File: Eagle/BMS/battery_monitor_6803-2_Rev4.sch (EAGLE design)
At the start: 66 parts, among them Q1 MOSFET-PCHANNELIRLML2244, Q10 IRF9530, Q2 MOSFET-NCHANNELBSS138, Q3 MOSFET-PCHANNELIRLML2244, Q4 MOSFET-PCHANNELIRLML2244, Q5 MOSFET-PCHANNELIRLML2244, Q6 MOSFET-NCHANNELBSS138, Q7 MOSFET-NCHANNELBSS138, Q8 MOSFET-NCHANNELBSS138, Q9 PMOS_AO4435

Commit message: Finished new BMS boards in Eagle.
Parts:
- U$9: MPN (none) -> LTC6803IG-2#PBF; OC_NEWARK (none) -> 27T5837
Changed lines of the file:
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@@
 </part>
 <part name="SUPPLY19" library="supply2" deviceset="GND" device=""/>
-<part name="U$9" library="Clayton" deviceset="LTC6803_BREAKOUT" device="" value="LTC6803"/>
+<part name="U$9" library="Clayton" deviceset="LTC6803_BREAKOUT" device="" value="LTC6803">
+<attribute name="MF" value=""/>
+<attribute name="MPN" value="LTC6803IG-2#PBF"/>
+<attribute name="OC_NEWARK" value="27T5837"/>
+</part>
 </parts>
 <sheets>
@@
 </instance>
 <instance part="SUPPLY19" gate="GND" x="170.18" y="66.04"/>
-<instance part="U$9" gate="G$1" x="165.1" y="-86.36"/>
+<instance part="U$9" gate="G$1" x="165.1" y="-86.36">
+<attribute name="OC_NEWARK" x="165.1" y="-86.36" size="1.778" layer="96" display="off"/>
+<attribute name="MF" x="165.1" y="-86.36" size="1.778" layer="96" display="off"/>
+<attribute name="MPN" x="165.1" y="-86.36" size="1.778" layer="96" display="off"/>
+</instance>
 </instances>
 <busses>

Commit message: Latest BMS Rev3 and Rev4 edits.
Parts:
- Q1, Q3, Q4, Q5: MPN SI2369DS-T1-GE3 -> IRLML2244TRPBF; OC_NEWARK 40X8697 -> 40T7448
- R26: value 1MEG -> 1Meg
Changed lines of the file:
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@@
 <part name="Q3" library="SparkFun-DiscreteSemi" deviceset="MOSFET-PCHANNEL" device="IRLML2244">
 <attribute name="MF" value=""/>
-<attribute name="MPN" value="SI2369DS-T1-GE3"/>
-<attribute name="OC_NEWARK" value="40X8697"/>
+<attribute name="MPN" value="IRLML2244TRPBF"/>
+<attribute name="OC_NEWARK" value="40T7448"/>
 </part>
 <part name="DZ1" library="SparkFun-DiscreteSemi" deviceset="DIODE-ZENER" device="-BZT52" value="PDZ7.5B">
@@
 <part name="Q4" library="SparkFun-DiscreteSemi" deviceset="MOSFET-PCHANNEL" device="IRLML2244">
 <attribute name="MF" value=""/>
-<attribute name="MPN" value="SI2369DS-T1-GE3"/>
-<attribute name="OC_NEWARK" value="40X8697"/>
+<attribute name="MPN" value="IRLML2244TRPBF"/>
+<attribute name="OC_NEWARK" value="40T7448"/>
 </part>
 <part name="Q5" library="SparkFun-DiscreteSemi" deviceset="MOSFET-PCHANNEL" device="IRLML2244">
 <attribute name="MF" value=""/>
-<attribute name="MPN" value="SI2369DS-T1-GE3"/>
-<attribute name="OC_NEWARK" value="40X8697"/>
+<attribute name="MPN" value="IRLML2244TRPBF"/>
+<attribute name="OC_NEWARK" value="40T7448"/>
 </part>
 <part name="R4" library="SparkFun-Resistors" deviceset="3.3KOHM1/10W1%(0603)" device="" value="100">
@@
 <part name="Q1" library="SparkFun-DiscreteSemi" deviceset="MOSFET-PCHANNEL" device="IRLML2244">
 <attribute name="MF" value=""/>
-<attribute name="MPN" value="SI2369DS-T1-GE3"/>
-<attribute name="OC_NEWARK" value="40X8697"/>
+<attribute name="MPN" value="IRLML2244TRPBF"/>
+<attribute name="OC_NEWARK" value="40T7448"/>
 </part>
 <part name="R8" library="SparkFun-Resistors" deviceset="3.3KOHM1/10W1%(0603)" device="" value="100">
@@
 <attribute name="OC_NEWARK" value="12H8386"/>
 </part>
-<part name="R26" library="SparkFun-Resistors" deviceset="3.3KOHM1/10W1%(0603)" device="" value="1MEG">
+<part name="R26" library="SparkFun-Resistors" deviceset="3.3KOHM1/10W1%(0603)" device="" value="1Meg">
 <attribute name="MF" value=""/>
 <attribute name="MPN" value="ERJ-3EKF1004V"/>

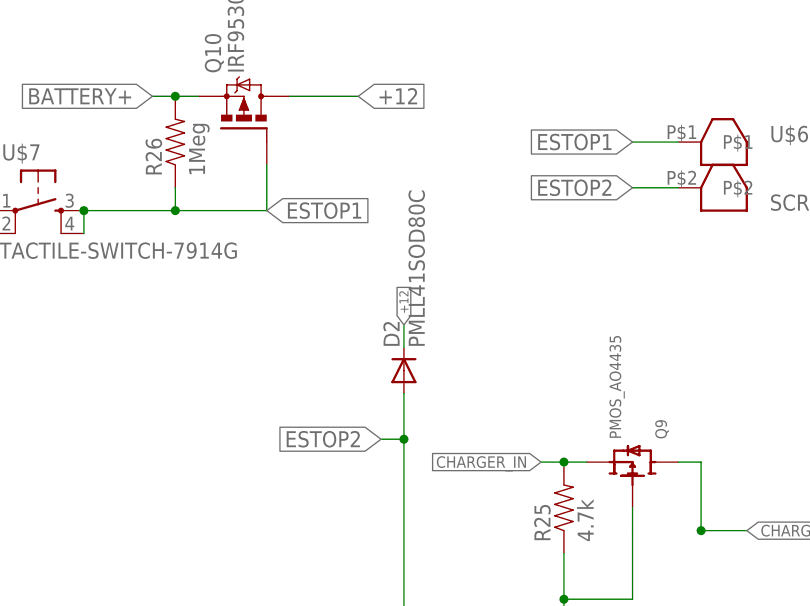
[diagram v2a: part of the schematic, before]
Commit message: Fixed minor issues with BMS board and added magnetic encoder information.
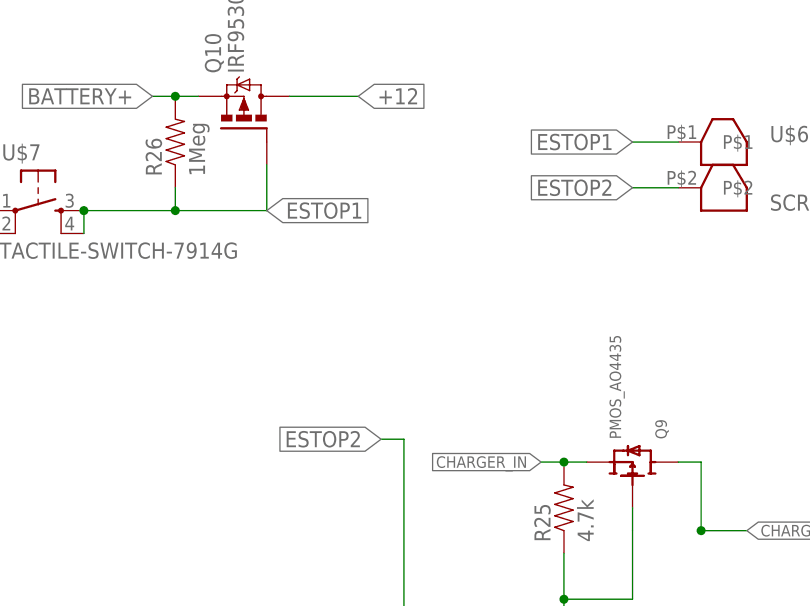
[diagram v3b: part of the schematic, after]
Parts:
- removed D2: PMLL41SOD80C, diode:PMLL41SOD80C
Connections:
- net +12: no longer D2.C
- net ESTOP2: no longer D2.A
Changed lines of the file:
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@@
 <part name="SUPPLY10" library="supply2" deviceset="GND" device=""/>
 <part name="SUPPLY11" library="supply2" deviceset="GND" device=""/>
-<part name="D2" library="diode" deviceset="PMLL41*" device="SOD80C">
-<attribute name="MF" value="FAIRCHILD SEMICONDUCTOR"/>
-<attribute name="MPN" value="FDLL4148"/>
-<attribute name="OC_NEWARK" value="18C6408"/>
-</part>
 <part name="I2C" library="isaac1" deviceset="SCREW_TERMINAL_2" device="">
 <attribute name="MF" value="TYCO ELECTRONICS"/>
@@
 <instance part="SUPPLY10" gate="GND" x="231.14" y="-2.54"/>
 <instance part="SUPPLY11" gate="GND" x="210.82" y="10.16"/>
-<instance part="D2" gate="G$1" x="223.52" y="60.96" rot="R90">
-<attribute name="OC_NEWARK" x="223.52" y="60.96" size="1.778" layer="96" display="off"/>
-<attribute name="MF" x="223.52" y="60.96" size="1.778" layer="96" display="off"/>
-<attribute name="MPN" x="223.52" y="60.96" size="1.778" layer="96" display="off"/>
-</instance>
 <instance part="I2C" gate="G$1" x="205.74" y="0">
 <attribute name="OC_NEWARK" x="205.74" y="0" size="1.778" layer="96" display="off"/>
@@
 </segment>
 <segment>
-<pinref part="D2" gate="G$1" pin="C"/>
-<wire x1="223.52" y1="63.5" x2="223.52" y2="66.04" width="0.1524" layer="91"/>
-<label x="223.52" y="66.04" size="1.016" layer="95" rot="R90" xref="yes"/>
-</segment>
-<segment>
 <pinref part="Q10" gate="G$1" pin="D"/>
 <wire x1="210.82" y1="91.44" x2="218.44" y2="91.44" width="0.1524" layer="91"/>
@@
 </segment>
 <segment>
-<pinref part="D2" gate="G$1" pin="A"/>
 <pinref part="Q6" gate="G$1" pin="D"/>
-<wire x1="223.52" y1="58.42" x2="223.52" y2="53.34" width="0.1524" layer="91"/>
 <wire x1="223.52" y1="53.34" x2="223.52" y2="27.94" width="0.1524" layer="91"/>
 <wire x1="223.52" y1="53.34" x2="220.98" y2="53.34" width="0.1524" layer="91"/>
-<junction x="223.52" y="53.34"/>
 <label x="220.98" y="53.34" size="1.778" layer="95" rot="R180" xref="yes"/>
 </segment>

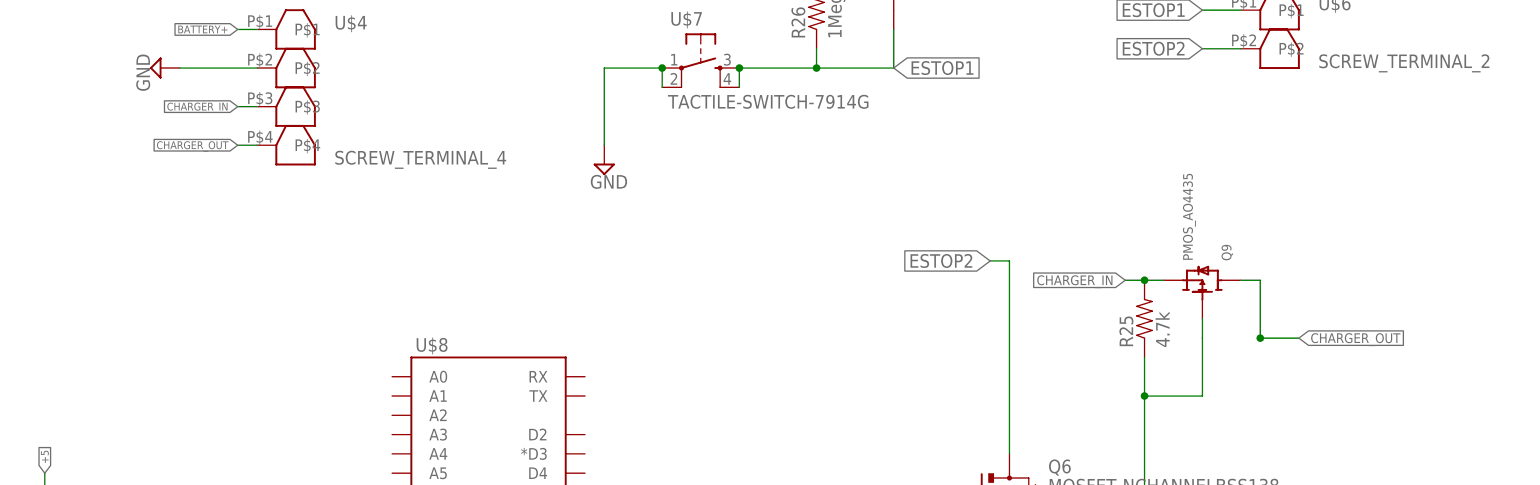
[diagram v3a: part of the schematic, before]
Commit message: Encoder design Rev1 changes.
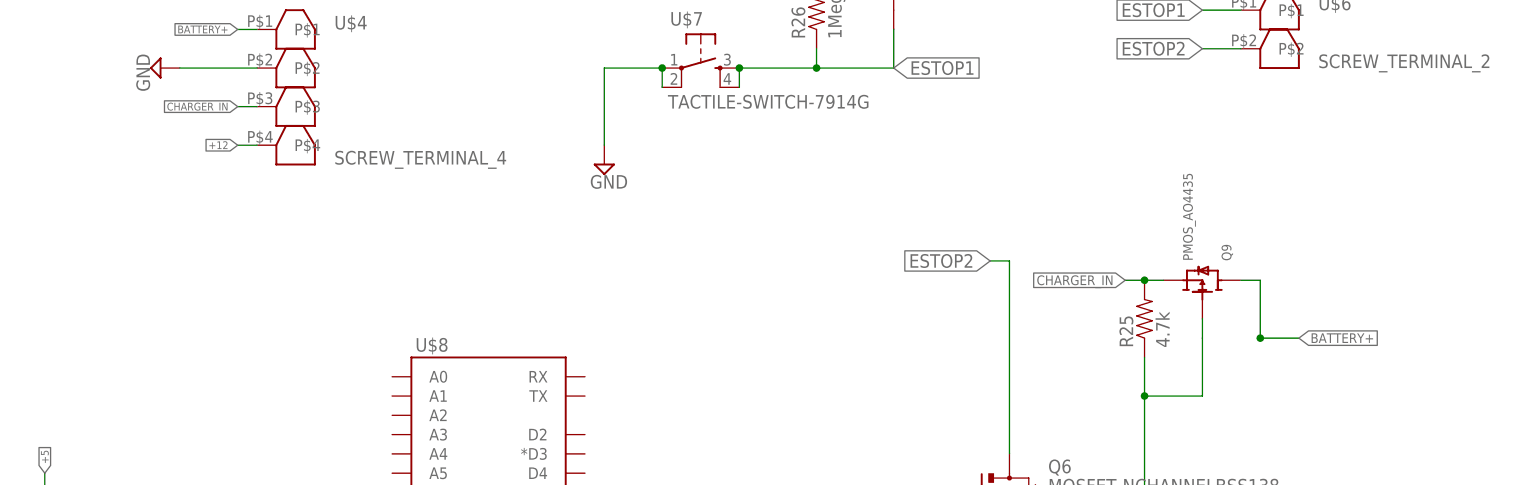
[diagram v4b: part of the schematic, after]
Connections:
- removed net CHARGER_OUT: Q9.DRAIN, U$4.P$4
- net +12: now also U$4.P$4
- net BATTERY+: now also Q9.DRAIN
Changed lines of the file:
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@@
 <label x="218.44" y="91.44" size="1.778" layer="95" xref="yes"/>
+</segment>
+<segment>
+<pinref part="U$4" gate="G$1" pin="P$4"/>
+<wire x1="124.46" y1="68.58" x2="121.92" y2="68.58" width="0.1524" layer="91"/>
+<label x="121.92" y="68.58" size="1.016" layer="95" rot="R180" xref="yes"/>
 </segment>
 </net>
@@
 </segment>
 </net>
-<net name="CHARGER_OUT" class="0">
+<net name="ESTOP2" class="0">
+<segment>
+<pinref part="U$6" gate="G$1" pin="P$2"/>
+<wire x1="254" y1="81.28" x2="248.92" y2="81.28" width="0.1524" layer="91"/>
+<label x="248.92" y="81.28" size="1.778" layer="95" rot="R180" xref="yes"/>
+</segment>
+<segment>
+<pinref part="Q6" gate="G$1" pin="D"/>
+<wire x1="223.52" y1="53.34" x2="223.52" y2="27.94" width="0.1524" layer="91"/>
+<wire x1="223.52" y1="53.34" x2="220.98" y2="53.34" width="0.1524" layer="91"/>
+<label x="220.98" y="53.34" size="1.778" layer="95" rot="R180" xref="yes"/>
+</segment>
+</net>
+<net name="BATTERY+" class="0">
+<segment>
+<pinref part="Q10" gate="G$1" pin="S"/>
+<wire x1="200.66" y1="91.44" x2="198.12" y2="91.44" width="0.1524" layer="91"/>
+<wire x1="198.12" y1="91.44" x2="195.58" y2="91.44" width="0.1524" layer="91"/>
+<junction x="198.12" y="91.44"/>
+<label x="195.58" y="91.44" size="1.778" layer="95" rot="R180" xref="yes"/>
+<pinref part="R26" gate="G$1" pin="2"/>
+</segment>
+<segment>
+<wire x1="124.46" y1="83.82" x2="121.92" y2="83.82" width="0.1524" layer="91"/>
+<label x="121.92" y="83.82" size="1.016" layer="95" rot="R180" xref="yes"/>
+<pinref part="U$4" gate="G$1" pin="P$1"/>
+</segment>
 <segment>
 <wire x1="256.54" y1="43.18" x2="261.62" y2="43.18" width="0.1524" layer="91"/>
@@
 <junction x="256.54" y="43.18"/>
 </segment>
-<segment>
-<pinref part="U$4" gate="G$1" pin="P$4"/>
-<wire x1="124.46" y1="68.58" x2="121.92" y2="68.58" width="0.1524" layer="91"/>
-<label x="121.92" y="68.58" size="1.016" layer="95" rot="R180" xref="yes"/>
-</segment>
-</net>
-<net name="ESTOP2" class="0">
-<segment>
-<pinref part="U$6" gate="G$1" pin="P$2"/>
-<wire x1="254" y1="81.28" x2="248.92" y2="81.28" width="0.1524" layer="91"/>
-<label x="248.92" y="81.28" size="1.778" layer="95" rot="R180" xref="yes"/>
-</segment>
-<segment>
-<pinref part="Q6" gate="G$1" pin="D"/>
-<wire x1="223.52" y1="53.34" x2="223.52" y2="27.94" width="0.1524" layer="91"/>
-<wire x1="223.52" y1="53.34" x2="220.98" y2="53.34" width="0.1524" layer="91"/>
-<label x="220.98" y="53.34" size="1.778" layer="95" rot="R180" xref="yes"/>
-</segment>
-</net>
-<net name="BATTERY+" class="0">
-<segment>
-<pinref part="Q10" gate="G$1" pin="S"/>
-<wire x1="200.66" y1="91.44" x2="198.12" y2="91.44" width="0.1524" layer="91"/>
-<wire x1="198.12" y1="91.44" x2="195.58" y2="91.44" width="0.1524" layer="91"/>
-<junction x="198.12" y="91.44"/>
-<label x="195.58" y="91.44" size="1.778" layer="95" rot="R180" xref="yes"/>
-<pinref part="R26" gate="G$1" pin="2"/>
-</segment>
-<segment>
-<wire x1="124.46" y1="83.82" x2="121.92" y2="83.82" width="0.1524" layer="91"/>
-<label x="121.92" y="83.82" size="1.016" layer="95" rot="R180" xref="yes"/>
-<pinref part="U$4" gate="G$1" pin="P$1"/>
-</segment>
-</net>
+</net>
